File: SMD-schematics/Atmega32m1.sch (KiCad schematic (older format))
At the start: 34 parts, among them J10 Conn_02x03_Odd_Even, J11 Conn_02x06_Odd_Even, J12 Conn_02x06_Odd_Even, J7 Conn_02x06_Odd_Even, J8 Conn_02x06_Odd_Even, J9 DB9_Female, SW1 SW_Push_Dual, SW2 SW_Push_Dual, SW3 SW_Push_Dual, U2 ATMEGA32M1-AU, U5 MAX232, Y2 16Mhz

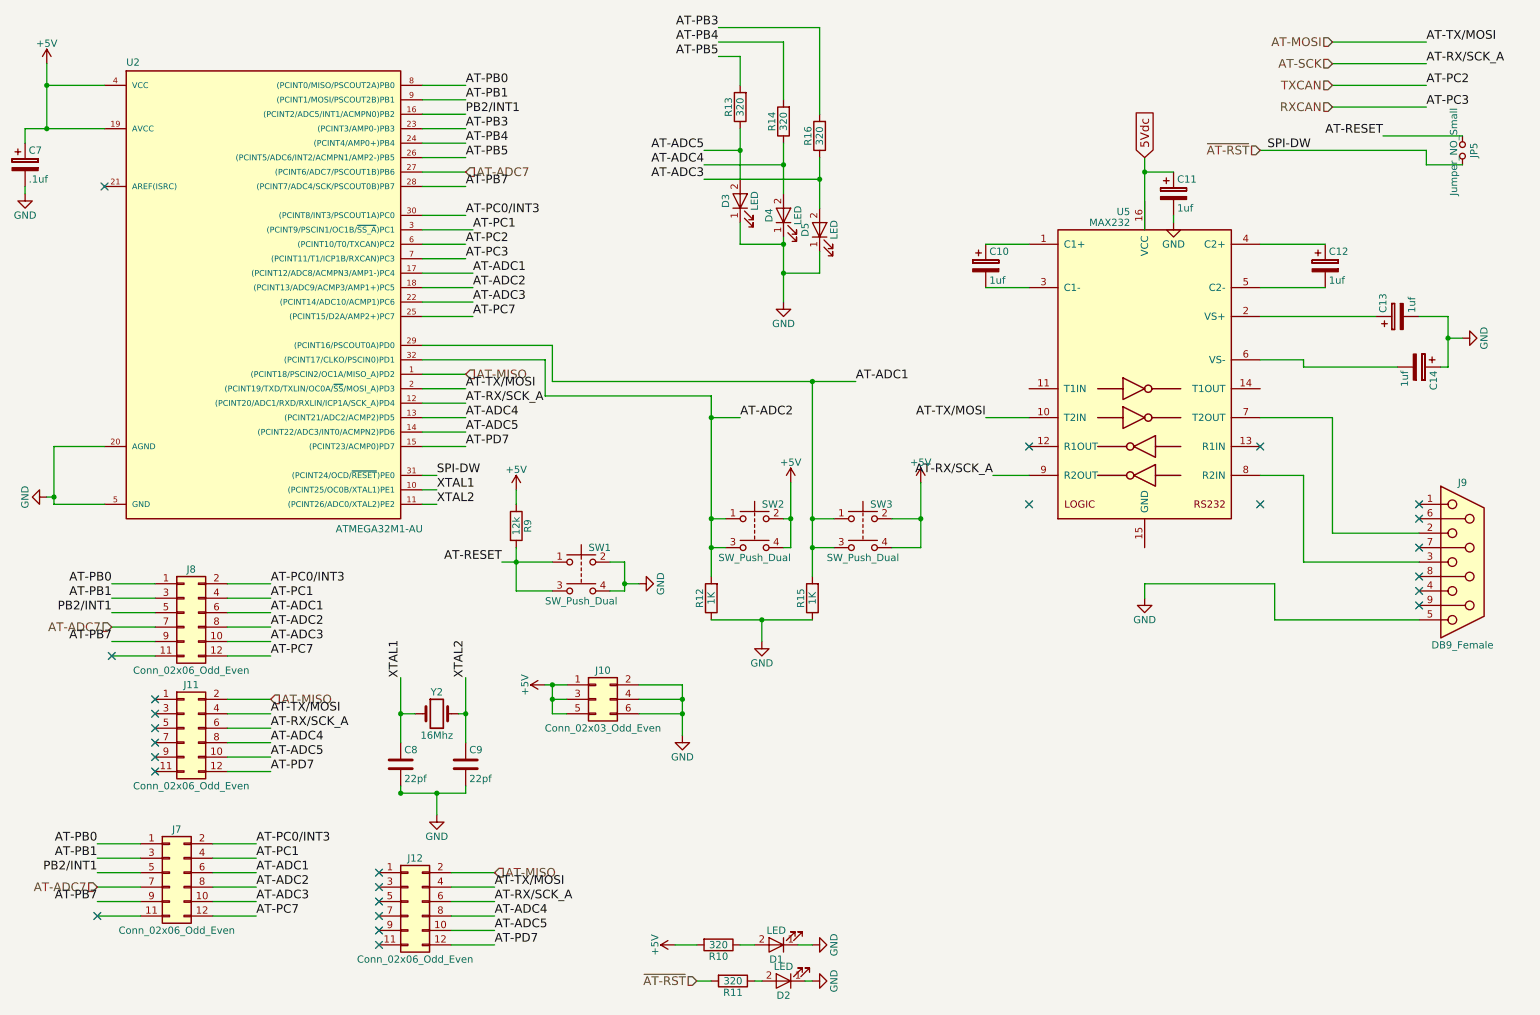
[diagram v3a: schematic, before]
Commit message: Updating Schematics: removing DB9 connectors and usart Transceiver
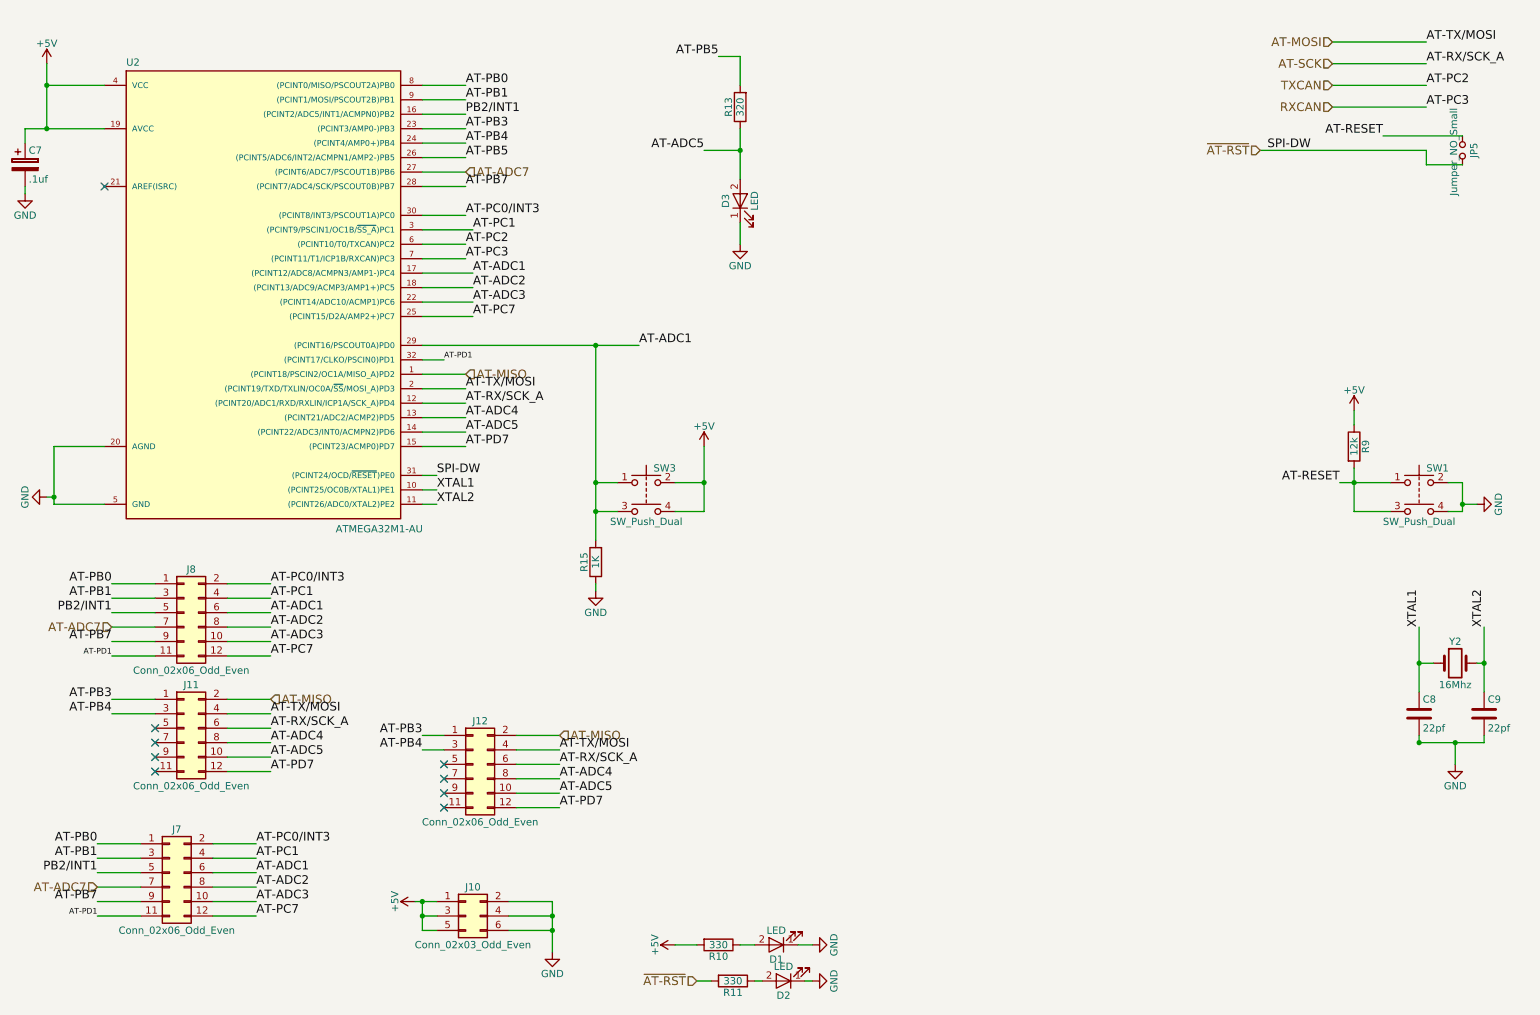
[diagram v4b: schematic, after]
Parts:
- removed C10, C11, C12, C13, C14: 1uf, Capacitors_SMD:CP_Elec_8x6.5, symbol CP
- removed D4, D5: LED, LEDs:LED_0805_HandSoldering, symbol LED
- removed J9: DB9_Female, Connectors_DSub:DB9FC, symbol DB9_Female
- removed R12: 1K, Resistors_SMD:R_1206_HandSoldering, symbol R
- removed R14, R16: 320, Resistors_SMD:R_1206_HandSoldering, symbol R
- removed SW2: SW_Push_Dual, Buttons_Switches_THT:Push_E-Switch_KS01Q01, symbol SW_Push_Dual
- removed U5: MAX232, Housings_SOIC:SOIC-16_3.9x9.9mm_Pitch1.27mm, symbol MAX232
- R10, R11: value 320 -> 330
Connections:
- net AT-ADC2: no longer U2.32 ((PCINT17/CLKO/PSCIN0)PD1)
- net AT-PB3: now also J11.1 (Pin_1), J12.1 (Pin_1)
- net AT-PB4: now also J11.3 (Pin_3), J12.3 (Pin_3)
- net AT-PD1: now reaches J8.11 (Pin_11)
- net AT-PD1: now also J7.11 (Pin_11), U2.32 ((PCINT17/CLKO/PSCIN0)PD1)
- no-connect marks 25 -> 9
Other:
- moved on the sheet: C8, C9, J10, J12, R15, R9, SW1, SW3, Y2

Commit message: adding lin circuit to the schematic
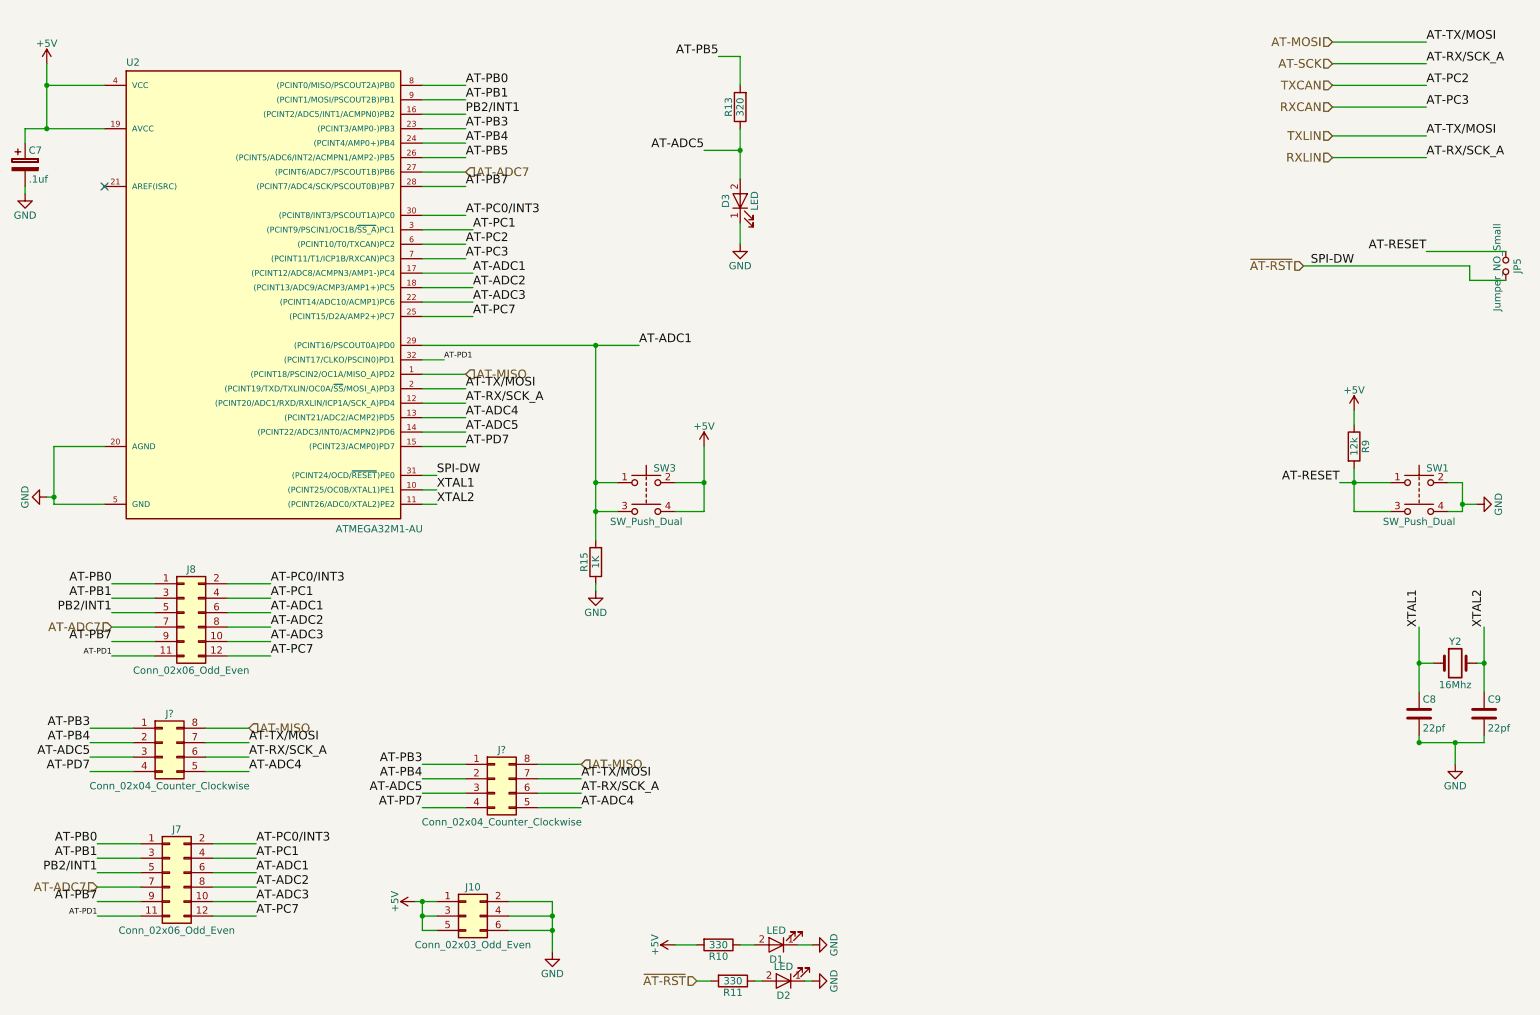
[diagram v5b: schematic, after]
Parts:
- removed J11, J12: Conn_02x06_Odd_Even, Pin_Headers:Pin_Header_Straight_2x06_Pitch2.54mm, symbol Conn_02x06_Odd_Even
- added J? (x2): Conn_02x04_Counter_Clockwise, symbol Conn_02x04_Counter_Clockwise
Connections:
- net AT-ADC4: now also J?.5 (Pin_5), J?.5 (Pin_5)
- net AT-ADC5: now also J?.3 (Pin_3), J?.3 (Pin_3)
- net AT-MISO: now also J?.8 (Pin_8), J?.8 (Pin_8)
- net AT-MOSI: now also J?.7 (Pin_7), J?.7 (Pin_7)
- net AT-PB3: now also J?.1 (Pin_1), J?.1 (Pin_1)
- net AT-PB4: now also J?.2 (Pin_2), J?.2 (Pin_2)
- net AT-PD7: now also J?.4 (Pin_4), J?.4 (Pin_4)
- net AT-SCK: now also J?.6 (Pin_6), J?.6 (Pin_6)
- no-connect marks 9 -> 1
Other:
- moved on the sheet: JP5
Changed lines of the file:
@@
 LIBS:contrib
 LIBS:valves
+LIBS:mcp2021
+LIBS:diod
+LIBS:diode
+LIBS:Diode1
 LIBS:Canboard-cache
 EELAYER 25 0
@@
 	1    0    0    -1
 $EndComp
-Text HLabel 9250 1850 0    60   Input ~ 0
+Text HLabel 9550 2650 0    60   Input ~ 0
 ~AT-RST
 $Comp
@@
 Text Label 9800 4150 2    60   ~ 0
 AT-RESET
-Text Label 10100 1750 2    60   ~ 0
+Text Label 10400 2550 2    60   ~ 0
 AT-RESET
 Text Label 10400 1250 0    60   ~ 0
@@
 	5750 7600 5800 7600
 Wire Wire Line
-	9250 1850 10400 1850
+	9550 2650 10700 2650
 Wire Wire Line
 	3550 4100 3450 4100
 Wire Wire Line
-	10100 1750 10650 1750
+	10400 2550 10950 2550
 Wire Wire Line
 	3750 1500 3450 1500
@@
 Text Label 1300 5250 2    60   ~ 0
 AT-PB7
-Text Label 1300 5750 2    60   ~ 0
+Text Label 1150 5950 2    60   ~ 0
 AT-PB4
 Text Label 1300 5050 2    60   ~ 0
@@
 Text Label 5500 1200 2    60   ~ 0
 AT-PB5
-Text Label 1300 5650 2    60   ~ 0
+Text Label 1150 5850 2    60   ~ 0
 AT-PB3
 Wire Wire Line
@@
 Wire Wire Line
 	2400 5350 2100 5350
-Text HLabel 2400 5650 2    60   Input ~ 0
+Text HLabel 2250 5850 2    60   Input ~ 0
 AT-MISO
-$Comp
-L Conn_02x06_Odd_Even J11
-U 1 1 5AC16837
-P 1800 5850
-F 0 "J11" H 1850 6150 50  0000 C CNN
-F 1 "Conn_02x06_Odd_Even" H 1850 5450 50  0000 C CNN
-F 2 "Pin_Headers:Pin_Header_Straight_2x06_Pitch2.54mm" H 1800 5850 50  0001 C CNN
-F 3 "" H 1800 5850 50  0001 C CNN
-	1    1800 5850
-	1    0    0    -1
-$EndComp
-Text Label 2400 5950 0    60   ~ 0
+Text Label 2250 6150 0    60   ~ 0
 AT-ADC4
-Text Label 2400 6050 0    60   ~ 0
+Text Label 1150 6050 2    60   ~ 0
 AT-ADC5
-Text Label 2400 6150 0    60   ~ 0
+Text Label 1150 6150 2    60   ~ 0
 AT-PD7
-Text Label 2400 5750 0    60   ~ 0
+Text Label 2250 5950 0    60   ~ 0
 AT-TX/MOSI
-Text Label 2400 5850 0    60   ~ 0
+Text Label 2250 6050 0    60   ~ 0
 AT-RX/SCK_A
 Wire Wire Line
-	2100 6050 2400 6050
-Wire Wire Line
-	2400 5950 2100 5950
-Wire Wire Line
-	2400 6150 2100 6150
-Wire Wire Line
-	2400 5750 2100 5750
-Wire Wire Line
-	2400 5850 2100 5850
-Wire Wire Line
-	2400 5650 2100 5650
-NoConn ~ 1600 5850
-NoConn ~ 1600 5950
-NoConn ~ 1600 6050
-NoConn ~ 1600 6150
+	1450 6050 1150 6050
+Wire Wire Line
+	2250 6150 1950 6150
+Wire Wire Line
+	1150 6150 1450 6150
+Wire Wire Line
+	2250 5950 1950 5950
+Wire Wire Line
+	2250 6050 1950 6050
+Wire Wire Line
+	2250 5850 1950 5850
 $Comp
 L Conn_02x06_Odd_Even J7
@@
 Wire Wire Line
 	2300 7150 2000 7150
-Text HLabel 4400 5900 2    60   Input ~ 0
-AT-MISO
-$Comp
-L Conn_02x06_Odd_Even J12
-U 1 1 5AC188F3
-P 3800 6100
-F 0 "J12" H 3850 6400 50  0000 C CNN
-F 1 "Conn_02x06_Odd_Even" H 3850 5700 50  0000 C CNN
-F 2 "Pin_Headers:Pin_Header_Straight_2x06_Pitch2.54mm" H 3800 6100 50  0001 C CNN
-F 3 "" H 3800 6100 50  0001 C CNN
-	1    3800 6100
-	1    0    0    -1
-$EndComp
-Text Label 4400 6200 0    60   ~ 0
-AT-ADC4
-Text Label 4400 6300 0    60   ~ 0
-AT-ADC5
-Text Label 4400 6400 0    60   ~ 0
-AT-PD7
-Text Label 4400 6000 0    60   ~ 0
-AT-TX/MOSI
-Text Label 4400 6100 0    60   ~ 0
-AT-RX/SCK_A
-Wire Wire Line
-	4100 6300 4400 6300
-Wire Wire Line
-	4400 6200 4100 6200
-Wire Wire Line
-	4400 6400 4100 6400
-Wire Wire Line
-	4400 6000 4100 6000
-Wire Wire Line
-	4400 6100 4100 6100
-Wire Wire Line
-	4400 5900 4100 5900
-NoConn ~ 3600 6100
-NoConn ~ 3600 6200
-NoConn ~ 3600 6300
-NoConn ~ 3600 6400
 Text HLabel 5350 7600 0    60   Input ~ 0
 ~AT-RST
@@
 Text Label 10800 5150 1    60   ~ 0
 XTAL2
-Text Label 9600 1850 2    60   ~ 0
+Text Label 9900 2650 2    60   ~ 0
 SPI-DW
 $Comp
 L Jumper_NO_Small JP5
 U 1 1 5AC326E0
-P 10650 1850
-F 0 "JP5" H 10650 1930 50  0000 C CNN
-F 1 "Jumper_NO_Small" H 10660 1790 50  0000 C CNN
-F 2 "Pin_Headers:Pin_Header_Straight_1x02_Pitch2.54mm" H 10650 1850 50  0001 C CNN
-F 3 "" H 10650 1850 50  0001 C CNN
-	1    10650 1850
+P 10950 2650
+F 0 "JP5" H 10950 2730 50  0000 C CNN
+F 1 "Jumper_NO_Small" H 10960 2590 50  0000 C CNN
+F 2 "Pin_Headers:Pin_Header_Straight_1x02_Pitch2.54mm" H 10950 2650 50  0001 C CNN
+F 3 "" H 10950 2650 50  0001 C CNN
+	1    10950 2650
 	0    1    1    0
 $EndComp
 Wire Wire Line
-	10400 1850 10400 1950
-Wire Wire Line
-	10400 1950 10650 1950
+	10700 2650 10700 2750
+Wire Wire Line
+	10700 2750 10950 2750
 $Comp
 L Conn_02x03_Odd_Even J10
@@
 	4650 4850 4650 4900
 Wire Wire Line
-	1300 5650 1600 5650
-Wire Wire Line
-	1600 5750 1300 5750
-Text Label 3450 6000 2    60   ~ 0
+	1150 5850 1450 5850
+Wire Wire Line
+	1450 5950 1150 5950
+$Comp
+L Conn_02x04_Counter_Clockwise J?
+U 1 1 5AD50829
+P 1650 5950
+F 0 "J?" H 1700 6150 50  0000 C CNN
+F 1 "Conn_02x04_Counter_Clockwise" H 1700 5650 50  0000 C CNN
+F 2 "" H 1650 5950 50  0001 C CNN
+F 3 "" H 1650 5950 50  0001 C CNN
+	1    1650 5950
+	1    0    0    -1
+$EndComp
+Text Label 3450 6200 2    60   ~ 0
 AT-PB4
-Text Label 3450 5900 2    60   ~ 0
+Text Label 3450 6100 2    60   ~ 0
 AT-PB3
-Wire Wire Line
-	3450 5900 3600 5900
-Wire Wire Line
-	3600 6000 3450 6000
+Text HLabel 4550 6100 2    60   Input ~ 0
+AT-MISO
+Text Label 4550 6400 0    60   ~ 0
+AT-ADC4
+Text Label 3450 6300 2    60   ~ 0
+AT-ADC5
+Text Label 3450 6400 2    60   ~ 0
+AT-PD7
+Text Label 4550 6200 0    60   ~ 0
+AT-TX/MOSI
+Text Label 4550 6300 0    60   ~ 0
+AT-RX/SCK_A
+Wire Wire Line
+	3750 6300 3450 6300
+Wire Wire Line
+	4550 6400 4250 6400
+Wire Wire Line
+	3450 6400 3750 6400
+Wire Wire Line
+	4550 6200 4250 6200
+Wire Wire Line
+	4550 6300 4250 6300
+Wire Wire Line
+	4550 6100 4250 6100
+Wire Wire Line
+	3450 6100 3750 6100
+Wire Wire Line
+	3750 6200 3450 6200
+$Comp
+L Conn_02x04_Counter_Clockwise J?
+U 1 1 5AD50A52
+P 3950 6200
+F 0 "J?" H 4000 6400 50  0000 C CNN
+F 1 "Conn_02x04_Counter_Clockwise" H 4000 5900 50  0000 C CNN
+F 2 "" H 3950 6200 50  0001 C CNN
+F 3 "" H 3950 6200 50  0001 C CNN
+	1    3950 6200
+	1    0    0    -1
+$EndComp
+Text Label 10400 1750 0    60   ~ 0
+AT-TX/MOSI
+Text Label 10400 1900 0    60   ~ 0
+AT-RX/SCK_A
+Text HLabel 9750 1750 0    60   Input ~ 0
+TXLIN
+Text HLabel 9750 1900 0    60   Input ~ 0
+RXLIN
+Wire Wire Line
+	10400 1900 9750 1900
+Wire Wire Line
+	9750 1750 10400 1750
 $EndSCHEMATC

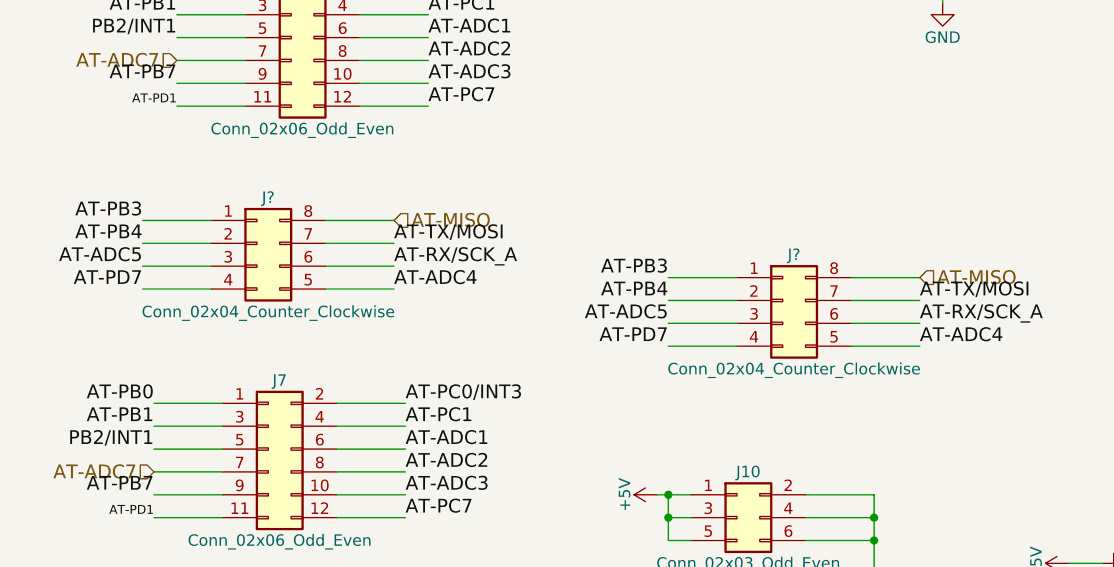
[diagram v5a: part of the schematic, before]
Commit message: adding lin circuit to the scgematic without the diode
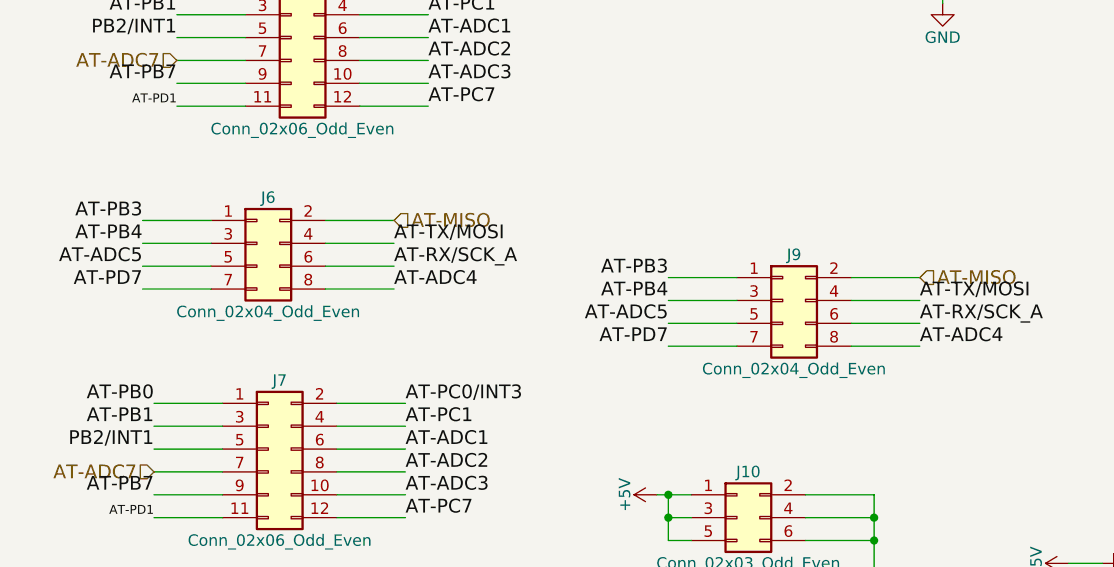
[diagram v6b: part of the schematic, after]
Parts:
- removed J? (x2): Conn_02x04_Counter_Clockwise, symbol Conn_02x04_Counter_Clockwise
- added J6, J9: Conn_02x04_Odd_Even, Pin_Headers:Pin_Header_Angled_2x04_Pitch2.54mm, symbol Conn_02x04_Odd_Even
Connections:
- net AT-ADC4: now also J6.8 (Pin_8), J9.8 (Pin_8)
- net AT-ADC5: now also J6.5 (Pin_5), J9.5 (Pin_5)
- net AT-MISO: now also J6.2 (Pin_2), J9.2 (Pin_2)
- net AT-MOSI: now also J6.4 (Pin_4), J9.4 (Pin_4)
- net AT-PB3: now also J6.1 (Pin_1), J9.1 (Pin_1)
- net AT-PB4: now also J6.3 (Pin_3), J9.3 (Pin_3)
- net AT-PD7: now also J6.7 (Pin_7), J9.7 (Pin_7)
- net AT-SCK: now also J6.6 (Pin_6), J9.6 (Pin_6)
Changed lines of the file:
@@
 Wire Wire Line
 	1450 5950 1150 5950
-$Comp
-L Conn_02x04_Counter_Clockwise J?
-U 1 1 5AD50829
-P 1650 5950
-F 0 "J?" H 1700 6150 50  0000 C CNN
-F 1 "Conn_02x04_Counter_Clockwise" H 1700 5650 50  0000 C CNN
-F 2 "" H 1650 5950 50  0001 C CNN
-F 3 "" H 1650 5950 50  0001 C CNN
-	1    1650 5950
-	1    0    0    -1
-$EndComp
 Text Label 3450 6200 2    60   ~ 0
 AT-PB4
@@
 Wire Wire Line
 	3750 6200 3450 6200
-$Comp
-L Conn_02x04_Counter_Clockwise J?
-U 1 1 5AD50A52
-P 3950 6200
-F 0 "J?" H 4000 6400 50  0000 C CNN
-F 1 "Conn_02x04_Counter_Clockwise" H 4000 5900 50  0000 C CNN
-F 2 "" H 3950 6200 50  0001 C CNN
-F 3 "" H 3950 6200 50  0001 C CNN
-	1    3950 6200
-	1    0    0    -1
-$EndComp
 Text Label 10400 1750 0    60   ~ 0
 AT-TX/MOSI
@@
 Wire Wire Line
 	9750 1750 10400 1750
+$Comp
+L Conn_02x04_Odd_Even J9
+U 1 1 5AD56421
+P 3950 6200
+F 0 "J9" H 4000 6400 50  0000 C CNN
+F 1 "Conn_02x04_Odd_Even" H 4000 5900 50  0000 C CNN
+F 2 "Pin_Headers:Pin_Header_Angled_2x04_Pitch2.54mm" H 3950 6200 50  0001 C CNN
+F 3 "" H 3950 6200 50  0001 C CNN
+	1    3950 6200
+	1    0    0    -1
+$EndComp
+$Comp
+L Conn_02x04_Odd_Even J6
+U 1 1 5AD564FE
+P 1650 5950
+F 0 "J6" H 1700 6150 50  0000 C CNN
+F 1 "Conn_02x04_Odd_Even" H 1700 5650 50  0000 C CNN
+F 2 "Pin_Headers:Pin_Header_Angled_2x04_Pitch2.54mm" H 1650 5950 50  0001 C CNN
+F 3 "" H 1650 5950 50  0001 C CNN
+	1    1650 5950
+	1    0    0    -1
+$EndComp
 $EndSCHEMATC
